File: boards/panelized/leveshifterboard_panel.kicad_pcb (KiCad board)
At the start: 2 copper layers, 82.6 x 43.2 mm, 40 parts, among them J1 RJ45, P1 CONN_2, P2 CONN_7, Q1 IRLR110, Q2 NDS355, SW1 SW_PUSH, U1 LM358, U2 SN74LVC1G74, U3 74HCT125, U4 TS2937

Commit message: Panelized boards
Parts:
- removed Q1: IRLR110, DPAK2
- added D5: ZENER_5.6V, sod123, F.Cu at (55.2, 31.8)
- added D6: ZENER_5.6V, sod123, F.Cu at (45.1, 30.5)
- added D7: ZENER_5.6V, sod123, F.Cu at (40.6, 45.7)
- added D8: ZENER_5.6V, sod123, F.Cu at (43.2, 45.7)
- added R13: 1k, SM0603, F.Cu at (41.3, 33.7)
- added R14: 1k, SM0603, F.Cu at (41.3, 36.2)
- added R15: 1k, SM0603, F.Cu at (41.3, 38.7)
- added R16: 1k, SM0603, F.Cu at (41.3, 41.3)
- added U5: BTS462, TO252-5L, F.Cu at (85.7, 51.4)
- C1: value 100n -> 100nF
- C2, C7: value 100nf -> 100nF
- F1: footprint fuse1 -> fuse22.5
- U2: value SN74LVC1G74 -> 74HC74; footprint SO8E -> SO14E
- moved C7 357.7 mm to (69.8, 33.0), turned to 90 degrees
- moved F1 354.5 mm to (35.6, 23.5)
- moved C3 348.6 mm to (54.6, 27.3), turned to 180 degrees
- moved 1PIN 348.3 mm to (19.1, 18.4)
- moved 1PIN 348.3 mm to (94.0, 18.4)
- moved 1PIN 348.3 mm to (94.0, 54.0)
- moved 1PIN 348.3 mm to (19.1, 54.0)
- moved C1 348.3 mm to (66.7, 41.3)
- moved C2 348.3 mm to (55.2, 44.5)
- moved C4 348.3 mm to (76.8, 19.1)
- moved C5 348.3 mm to (64.8, 27.3)
- moved C6 348.3 mm to (76.8, 29.8)
- moved D1 348.3 mm to (87.6, 33.7)
- moved D2 348.3 mm to (87.6, 31.8)
- moved D4 348.3 mm to (87.6, 29.8)
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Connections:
- J1 pad 10: Sense -> (no net)
- R8 pad 1: N-0000024 -> N-0000010
- SW1 pad 1: N-0000024 -> N-0000010
- U2 pad 1: GND -> N-0000010
- U2 pad 3: PowerOn -> GND
- U2 pad 4: GND -> Shutdown
- U2 pad 6: N-0000024 -> PowerOn
- U2 pad 7: Shutdown -> GND
- U2 pad 8: +5V -> (no net)
- U3 pad 11: Reset -> N-0000015
- U3 pad 3: Clock -> N-0000018
- U3 pad 6: Enable -> N-0000017
- U3 pad 8: Data_Out -> N-0000016
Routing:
- net N-0000029: track 7.62 -> 35.1 mm
- net N-0000024: track 26.8 -> 0.00 mm, vias 1 -> 0
- net N-0000010: track 0.00 -> 25.2 mm, vias 0 -> 1
- net N-0000016: track 0.00 -> 15.8 mm, vias 0 -> 3
- net Clock: track 23.8 -> 8.13 mm
- net N-0000018: track 0.00 -> 15.6 mm
- net N-0000015: track 0.00 -> 14.2 mm, vias 0 -> 2
- net N-0000017: track 0.00 -> 13.6 mm, vias 0 -> 2
- net Reset: track 20.5 -> 8.13 mm
- net PowerOn: track 26.2 -> 14.8 mm
- net Data_Out: track 19.1 -> 8.38 mm, vias 3 -> 1
- net Enable: track 18.6 -> 8.13 mm
- net +5V: track 86.6 -> 93.1 mm, vias 5 -> 3
- net +24V: track 110.0 -> 114.9 mm
- net Shutdown: track 16.8 -> 18.2 mm
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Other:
- board text added: "Version 1.1"
- board text removed: "Version 1.0"

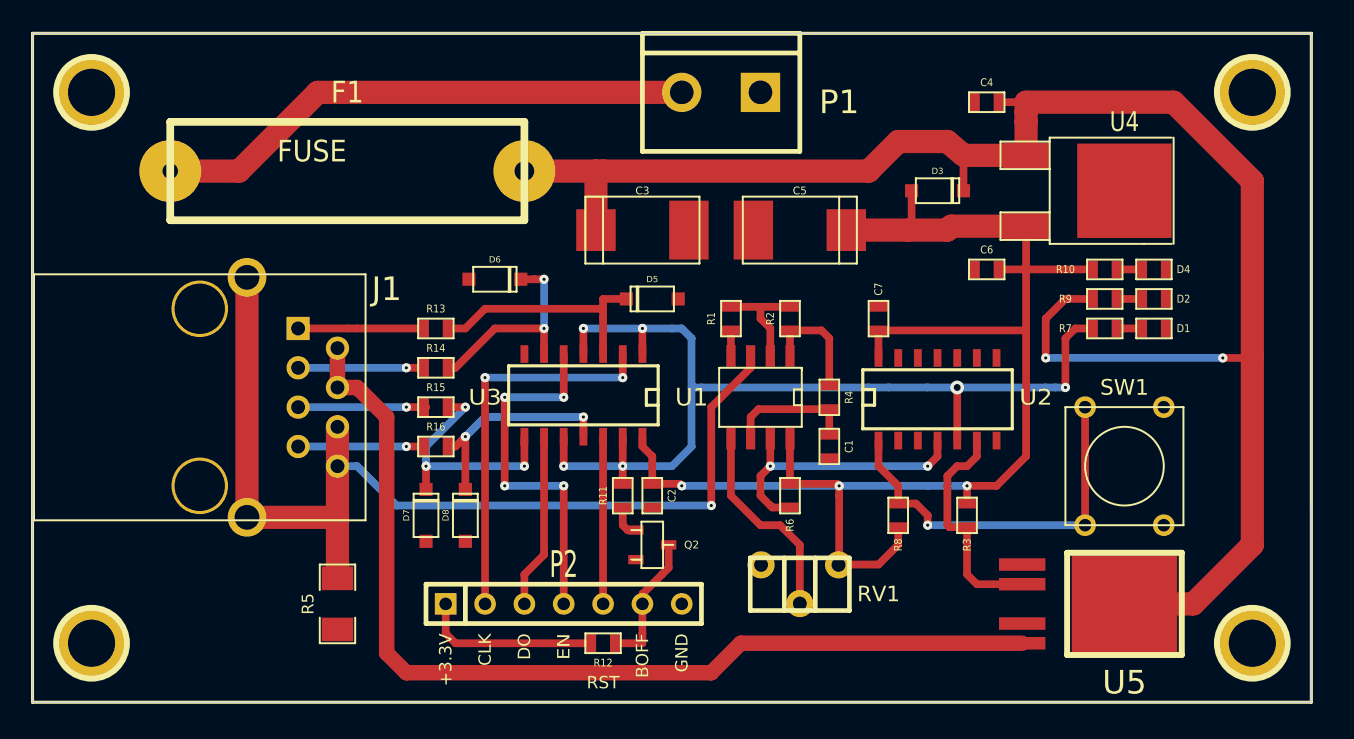
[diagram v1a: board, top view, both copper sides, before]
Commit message: Added logos
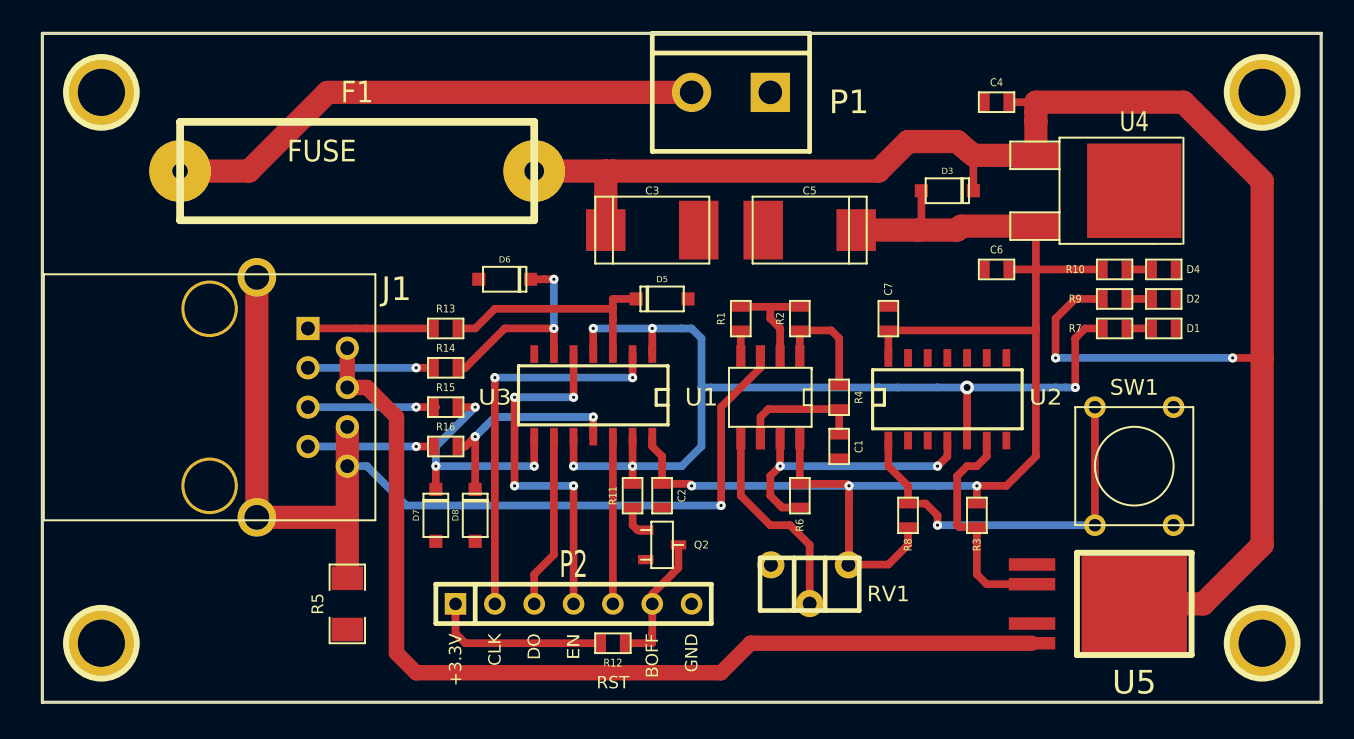
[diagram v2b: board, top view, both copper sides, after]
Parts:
- added G***: logo_hacker_silkbot_10_00mm, logo_hacker_silkbot_10_00mm, B.Cu at (35.6, 50.8)
- moved C1 0.64 mm to (67.3, 41.3)
- moved C2 0.64 mm to (55.9, 44.5)
- moved C4 0.64 mm to (77.5, 19.1)
- moved C5 0.64 mm to (65.4, 27.3)
- moved C6 0.64 mm to (77.5, 29.8)
- moved C7 0.64 mm to (70.5, 33.0)
- moved D1 0.64 mm to (88.3, 33.7)
- moved D2 0.64 mm to (88.3, 31.8)
- moved D3 0.64 mm to (74.3, 24.8)
- moved D4 0.64 mm to (88.3, 29.8)
- moved D5 0.64 mm to (55.9, 31.8)
- moved P1 0.64 mm to (60.3, 18.4)
- moved Q2 0.64 mm to (55.9, 47.6)
- moved R10 0.64 mm to (85.1, 29.8)
- moved R3 0.64 mm to (76.2, 45.7)
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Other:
- board size 82.6 x 43.2 mm -> 82.5 x 43.2 mm
